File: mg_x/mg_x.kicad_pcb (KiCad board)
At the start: 2 copper layers, 17 x 20 mm, 10 parts, among them IC1 TC118S, U1 ATtiny24-20SS, U2 LD3985G18R_TSOT23, U4 ACS712xLCTR-05B

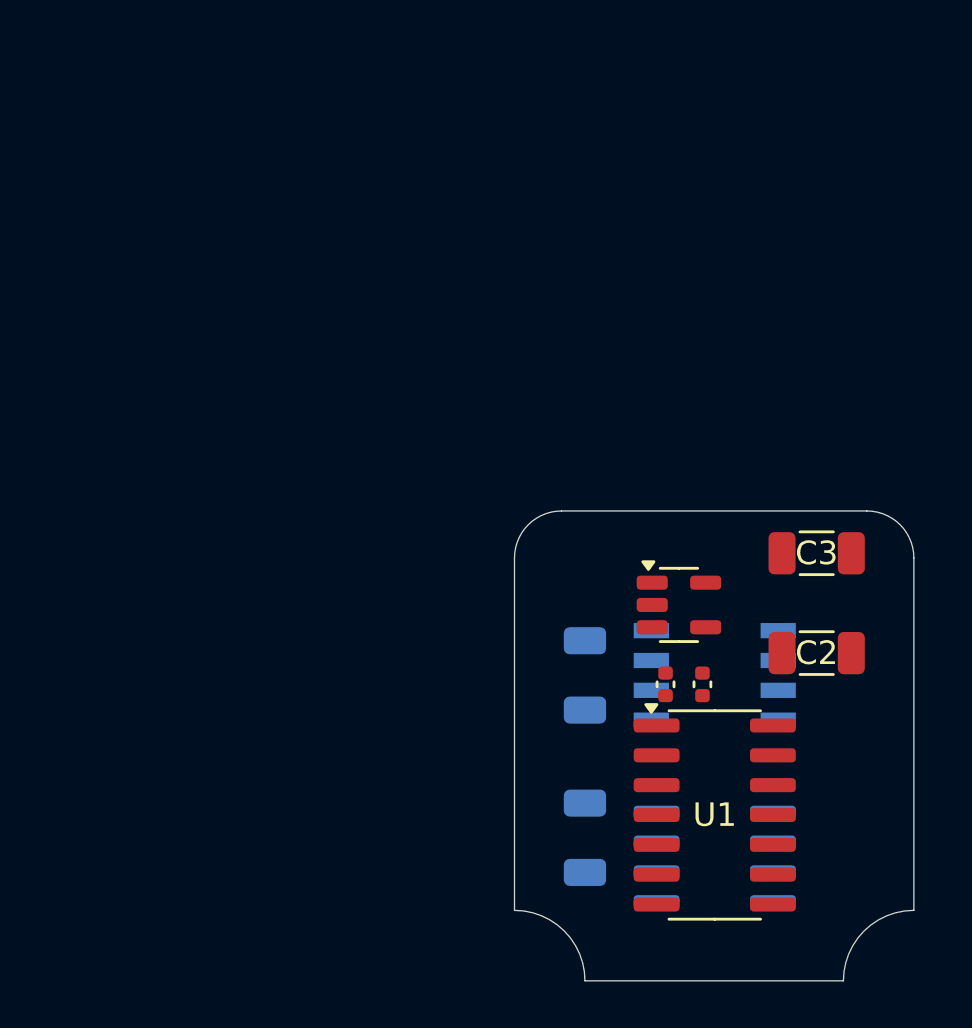
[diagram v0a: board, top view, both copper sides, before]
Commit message: Create footprint connector
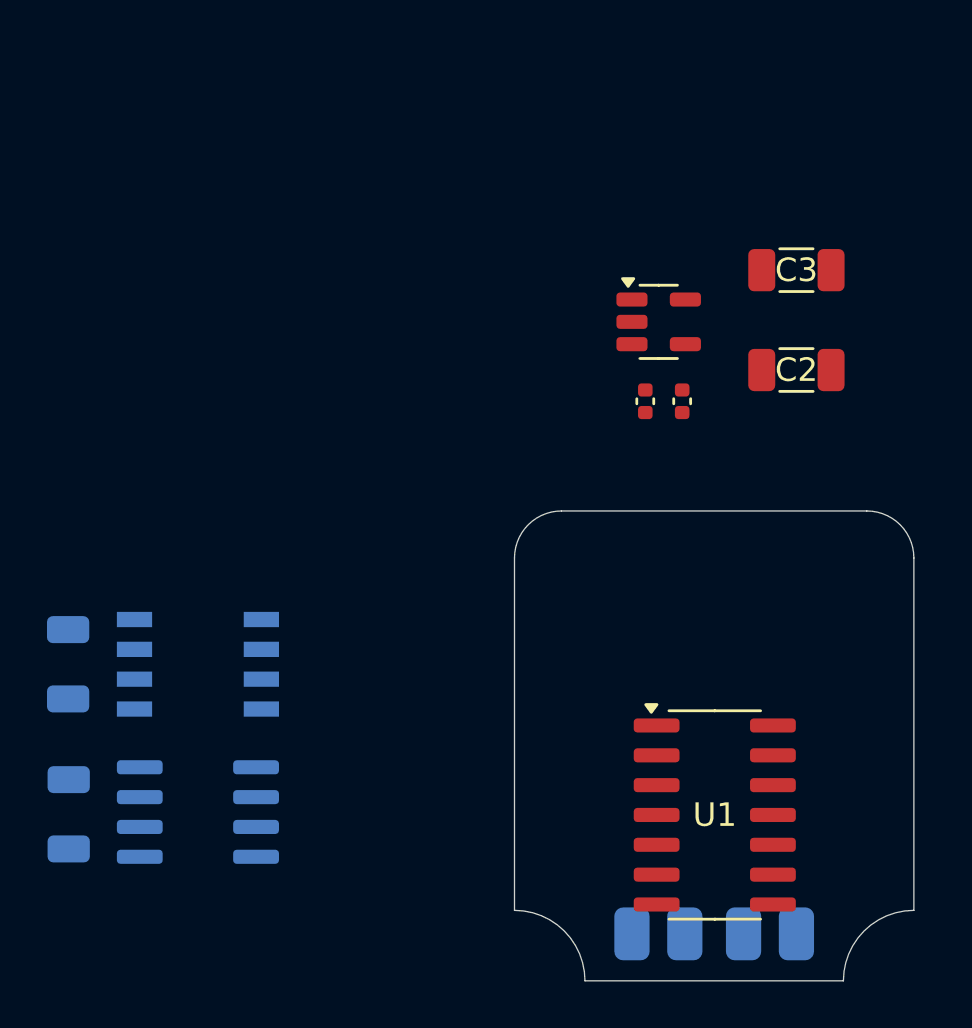
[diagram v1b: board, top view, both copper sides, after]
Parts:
- added J4: Conn_01x04, Connector_MG_X:Connector_User_Interface, B.Cu at (151.5, 107.0)
- moved U4 22.1 mm to (129.5, 101.8)
- moved C5 22.0 mm to (124.0, 95.5)
- moved IC1 22.0 mm to (129.5, 95.5)
- moved C1 22.0 mm to (124.0, 101.9)
- moved C2 12.1 mm to (155.0, 83.0)
- moved C3 12.1 mm to (155.0, 78.8)
- moved C4 12.1 mm to (150.1, 84.3)
- moved C6 12.1 mm to (148.6, 84.3)
- moved U2 12.1 mm to (149.1, 81.0)
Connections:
- U1 pad 1: unconnected-(U1-VCC-Pad1) -> +3.3V
- U1 pad 14: unconnected-(U1-GND-Pad14) -> GND
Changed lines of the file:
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@@
 	(net 7 "unconnected-(U1-PA5-Pad8)")
 	(net 8 "unconnected-(U1-XTAL2{slash}PB1-Pad3)")
-	(net 9 "unconnected-(U1-VCC-Pad1)")
+	(net 9 "unconnected-(J4-Pin_4-Pad4)")
 	(net 10 "unconnected-(U1-PB2-Pad5)")
 	(net 11 "unconnected-(U1-PA2-Pad11)")
@@
 	(net 18 "unconnected-(U1-PA6-Pad7)")
 	(net 19 "+3.3V")
-	(net 20 "unconnected-(U1-GND-Pad14)")
+	(net 20 "unconnected-(J4-Pin_1-Pad1)")
 	(net 21 "unconnected-(U1-AREF{slash}PA0-Pad13)")
 	(net 22 "Net-(U4-FILTER)")
@@
 	(net 26 "Net-(U2-BYP)")
 	(net 27 "Net-(U2-INH)")
+	(net 28 "unconnected-(J4-Pin_3-Pad3)")
+	(net 29 "unconnected-(J4-Pin_2-Pad2)")
 	(footprint "Capacitor_SMD:C_1206_3216Metric"
 		(layer "F.Cu")
-		(at 155.8625 90.8)
+		(at 155 78.75)
 		(descr "Capacitor SMD 1206 (3216 Metric), square (rectangular) end terminal, IPC_7351 nominal, (Body size source: IPC-SM-782 page 76, https://www.pcb-3d.com/wordpress/wp-content/uploads/ipc-sm-782a_amendment_1_and_2.pdf), generated with kicad-footprint-generator")
 		(tags "capacitor")
@@
 			)
 		)
-		(property ki_fp_filters "C_*")
-		(sheetname "Root")
-		(sheetfile "mg_x.kicad_sch")
 		(attr smd)
 		(fp_line
@@
 	(footprint "Capacitor_SMD:C_1206_3216Metric"
 		(layer "F.Cu")
-		(at 155.8625 95.05)
+		(at 155 83)
 		(descr "Capacitor SMD 1206 (3216 Metric), square (rectangular) end terminal, IPC_7351 nominal, (Body size source: IPC-SM-782 page 76, https://www.pcb-3d.com/wordpress/wp-content/uploads/ipc-sm-782a_amendment_1_and_2.pdf), generated with kicad-footprint-generator")
 		(tags "capacitor")
@@
 			)
 		)
-		(property ki_fp_filters "C_*")
-		(sheetname "Root")
-		(sheetfile "mg_x.kicad_sch")
 		(attr smd)
 		(fp_line
@@
 	(footprint "Capacitor_SMD:C_0402_1005Metric"
 		(layer "F.Cu")
-		(at 149.43 96.38 -90)
+		(at 148.5675 84.33 -90)
 		(descr "Capacitor SMD 0402 (1005 Metric), square (rectangular) end terminal, IPC_7351 nominal, (Body size source: IPC-SM-782 page 76, https://www.pcb-3d.com/wordpress/wp-content/uploads/ipc-sm-782a_amendment_1_and_2.pdf), generated with kicad-footprint-generator")
 		(tags "capacitor")
@@
 			)
 		)
-		(property ki_fp_filters "C_*")
-		(sheetname "Root")
-		(sheetfile "mg_x.kicad_sch")
 		(attr smd)
 		(fp_line
@@
 	(footprint "Package_TO_SOT_SMD:TSOT-23-5"
 		(layer "F.Cu")
-		(at 150 93)
+		(at 149.1375 80.95)
 		(descr "TSOT, 5 Pin (https://www.jedec.org/sites/default/files/docs/MO-193D.pdf variant AB), generated with kicad-footprint-generator ipc_gullwing_generator.py")
 		(tags "TSOT TO_SOT_SMD")
@@
 			)
 		)
-		(property ki_fp_filters "TSOT?23*")
-		(sheetname "Root")
-		(sheetfile "mg_x.kicad_sch")
 		(attr smd)
 		(fp_line
@@
 	(footprint "Capacitor_SMD:C_0402_1005Metric"
 		(layer "F.Cu")
-		(at 151 96.38 -90)
+		(at 150.1375 84.33 -90)
 		(descr "Capacitor SMD 0402 (1005 Metric), square (rectangular) end terminal, IPC_7351 nominal, (Body size source: IPC-SM-782 page 76, https://www.pcb-3d.com/wordpress/wp-content/uploads/ipc-sm-782a_amendment_1_and_2.pdf), generated with kicad-footprint-generator")
 		(tags "capacitor")
@@
 			)
 		)
-		(property ki_fp_filters "C_*")
-		(sheetname "Root")
-		(sheetfile "mg_x.kicad_sch")
 		(attr smd)
 		(fp_line
@@
 			)
 		)
-		(property ki_fp_filters "SOIC*3.9x8.7mm*P1.27mm*")
-		(sheetname "Root")
-		(sheetfile "mg_x.kicad_sch")
 		(attr smd)
 		(fp_line
@@
 			(layers "F.Cu" "F.Paste" "F.Mask")
 			(roundrect_rratio 0.25)
-			(net 9 "unconnected-(U1-VCC-Pad1)")
+			(net 19 "+3.3V")
 			(pinfunction "VCC")
 			(pintype "power_in")
@@
 			(layers "F.Cu" "F.Paste" "F.Mask")
 			(roundrect_rratio 0.25)
-			(net 20 "unconnected-(U1-GND-Pad14)")
+			(net 1 "GND")
 			(pinfunction "GND")
 			(pintype "power_in")
@@
 	(footprint "Capacitor_SMD:C_1206_3216Metric"
 		(layer "B.Cu")
-		(at 146 102.91 90)
+		(at 124.025 101.91 90)
 		(descr "Capacitor SMD 1206 (3216 Metric), square (rectangular) end terminal, IPC_7351 nominal, (Body size source: IPC-SM-782 page 76, https://www.pcb-3d.com/wordpress/wp-content/uploads/ipc-sm-782a_amendment_1_and_2.pdf), generated with kicad-footprint-generator")
 		(tags "capacitor")
 		(property "Reference" "C1"
-			(at 0 0 270)
+			(at 0 0 -90)
 			(layer "B.SilkS")
 			(effects
@@
 		)
 		(property "Value" "1nF"
-			(at 0 -1.85 270)
+			(at 0 -1.85 -90)
 			(layer "B.Fab")
 			(hide yes)
@@
 			)
 		)
-		(property ki_fp_filters "C_*")
-		(sheetname "Root")
-		(sheetfile "mg_x.kicad_sch")
 		(attr smd)
 		(fp_line
@@
 		)
 		(fp_text user "${REFERENCE}"
-			(at 0 0 270)
+			(at 0 0 -90)
 			(layer "B.Fab")
 			(effects
@@
 	(footprint "Capacitor_SMD:C_1206_3216Metric"
 		(layer "B.Cu")
-		(at 146 96 -90)
+		(at 124 95.525 -90)
 		(descr "Capacitor SMD 1206 (3216 Metric), square (rectangular) end terminal, IPC_7351 nominal, (Body size source: IPC-SM-782 page 76, https://www.pcb-3d.com/wordpress/wp-content/uploads/ipc-sm-782a_amendment_1_and_2.pdf), generated with kicad-footprint-generator")
 		(tags "capacitor")
@@
 			)
 		)
-		(property ki_fp_filters "C_*")
-		(sheetname "Root")
-		(sheetfile "mg_x.kicad_sch")
 		(attr smd)
 		(fp_line
@@
 	(footprint "Package_SO:SOIC-8_3.9x4.9mm_P1.27mm"
 		(layer "B.Cu")
-		(at 151.525 103.75 180)
+		(at 129.525 101.815 180)
 		(descr "SOIC, 8 Pin (JEDEC MS-012AA, https://www.analog.com/media/en/package-pcb-resources/package/pkg_pdf/soic_narrow-r/r_8.pdf), generated with kicad-footprint-generator ipc_gullwing_generator.py")
 		(tags "SOIC SO")
@@
 			)
 		)
-		(property ki_fp_filters "SOIC*3.9x4.9m*P1.27mm*")
-		(sheetname "Root")
-		(sheetfile "mg_x.kicad_sch")
 		(attr smd)
 		(fp_line
@@
 		)
 	)
+	(footprint "Connector_MG_X:Connector_User_Interface"
+		(layer "B.Cu")
+		(at 151.5 107 180)
+		(property "Reference" "J4"
+			(at 0 2 0)
+			(unlocked yes)
+			(layer "B.SilkS")
+			(hide yes)
+			(effects
+				(font
+					(size 1 1)
+					(thickness 0.1)
+				)
+				(justify mirror)
+			)
+		)
+		(property "Value" "Conn_01x04"
+			(at 0 -1 0)
+			(unlocked yes)
+			(layer "B.Fab")
+			(hide yes)
+			(effects
+				(font
+					(size 1 1)
+					(thickness 0.15)
+				)
+				(justify mirror)
+			)
+		)
+		(property "Footprint" "Connector_MG_X:Connector_User_Interface"
+			(at 0 0 0)
+			(unlocked yes)
+			(layer "B.Fab")
+			(hide yes)
+			(effects
+				(font
+					(size 1 1)
+					(thickness 0.15)
+				)
+				(justify mirror)
+			)
+		)
+		(property "Datasheet" ""
+			(at 0 0 0)
+			(unlocked yes)
+			(layer "B.Fab")
+			(hide yes)
+			(effects
+				(font
+					(size 1 1)
+					(thickness 0.15)
+				)
+				(justify mirror)
+			)
+		)
+		(property "Description" "Generic connector, single row, 01x04, script generated (kicad-library-utils/schlib/autogen/connector/)"
+			(at 0 0 0)
+			(unlocked yes)
+			(layer "B.Fab")
+			(hide yes)
+			(effects
+				(font
+					(size 1 1)
+					(thickness 0.15)
+				)
+				(justify mirror)
+			)
+		)
+		(attr smd)
+		(fp_line
+			(start 3.5 1.5)
+			(end -3.5 1.5)
+			(stroke
+				(width 0.1)
+				(type default)
+			)
+			(layer "B.SilkS")
+		)
+		(fp_text user "${REFERENCE}"
+			(at 0 -2.5 0)
+			(unlocked yes)
+			(layer "B.Fab")
+			(effects
+				(font
+					(size 1 1)
+					(thickness 0.15)
+				)
+				(justify mirror)
+			)
+		)
+		(pad "1" smd roundrect
+			(at -3.5 0 180)
+			(size 1.5 2.25)
+			(layers "B.Cu" "B.Paste" "B.Mask")
+			(roundrect_rratio 0.25)
+			(net 20 "unconnected-(J4-Pin_1-Pad1)")
+			(pinfunction "Pin_1")
+			(pintype "passive")
+			(thermal_bridge_angle 45)
+		)
+		(pad "2" smd roundrect
+			(at -1.25 0 180)
+			(size 1.5 2.25)
+			(layers "B.Cu" "B.Paste" "B.Mask")
+			(roundrect_rratio 0.25)
+			(net 29 "unconnected-(J4-Pin_2-Pad2)")
+			(pinfunction "Pin_2")
+			(pintype "passive")
+			(thermal_bridge_angle 45)
+		)
+		(pad "3" smd roundrect
+			(at 1.25 0 180)
+			(size 1.5 2.25)
+			(layers "B.Cu" "B.Paste" "B.Mask")
+			(roundrect_rratio 0.25)
+			(net 28 "unconnected-(J4-Pin_3-Pad3)")
+			(pinfunction "Pin_3")
+			(pintype "passive")
+			(thermal_bridge_angle 45)
+		)
+		(pad "4" smd roundrect
+			(at 3.5 0 180)
+			(size 1.5 2.25)
+			(layers "B.Cu" "B.Paste" "B.Mask")
+			(roundrect_rratio 0.25)
+			(net 9 "unconnected-(J4-Pin_4-Pad4)")
+			(pinfunction "Pin_4")
+			(pintype "passive")
+			(thermal_bridge_angle 45)
+		)
+	)
 	(footprint "TC118S:SOIC127P600X155-8N"
 		(layer "B.Cu")
-		(at 151.525 96 180)
+		(at 129.525 95.525 180)
 		(descr "sop8")
 		(tags "Integrated Circuit")
@@
 			)
 		)
-		(sheetname "Root")
-		(sheetfile "mg_x.kicad_sch")
 		(attr smd)
 		(fp_line

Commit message: Minor changes in PCB
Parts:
- added J1: Conn_01x02, Connector_MG_X:Connector_Motor_DC, B.Cu at (151.5, 91.7)
- added J2: Conn_01x03, Connector_MG_X:Connector_Sensor_Signal, F.Cu at (151.5, 90.9)
- added J3: Conn_01x03, Connector_MG_X:Connector_Sensor_Signal, F.Cu at (151.5, 94.7)
- C2, C3, C4, C6, U2: moved to B.Cu
- moved C6 12.3 mm to (160.2, 80.2), turned to 90 degrees
- moved C4 10.3 mm to (160.2, 82.1), turned to 90 degrees
- moved U2 8.72 mm to (157.8, 81.3), turned to -90 degrees
- moved C3 4.81 mm to (153.6, 83.4), turned to 180 degrees
- moved C2 2.94 mm to (153.6, 80.4), turned to 180 degrees
- moved C1 0.93 mm to (124.0, 101.0)
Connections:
- J4 pad 1: unconnected-(J4-Pin_1-Pad1) -> VCC
- J4 pad 2: unconnected-(J4-Pin_2-Pad2) -> /SDA
- J4 pad 3: unconnected-(J4-Pin_3-Pad3) -> /SCL
- J4 pad 4: unconnected-(J4-Pin_4-Pad4) -> GND
- U1 pad 2: unconnected-(U1-XTAL1/PB0-Pad2) -> /SCL
- U1 pad 3: unconnected-(U1-XTAL2/PB1-Pad3) -> /SDA

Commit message: Improved PCB
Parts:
- moved C1 42.7 mm to (153.5, 70.2), turned to 0 degrees
- moved C5 37.6 mm to (158.3, 80.0), turned to 90 degrees
- moved U4 35.0 mm to (147.2, 71.7), turned to 0 degrees
- moved IC1 27.7 mm to (152.6, 80.2), turned to 0 degrees
- moved J1 20.2 mm to (157.8, 72.5), turned to 90 degrees
- moved C6 16.2 mm to (144.5, 76.0), turned to 0 degrees
- moved C4 14.7 mm to (146.8, 76.0), turned to 180 degrees
- moved U2 12.4 mm to (145.6, 79.0), turned to 0 degrees
- moved C3 10.1 mm to (153.5, 73.2), turned to 0 degrees
- moved C2 8.17 mm to (145.9, 83.0), turned to 0 degrees
- moved U1 3.01 mm to (154.5, 101.5)
- moved J2 3.00 mm to (154.5, 91.0)
- moved J3 3.00 mm to (154.5, 94.8)
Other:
- copper layers 2 -> 4
